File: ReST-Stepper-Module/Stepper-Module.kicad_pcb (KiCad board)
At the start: 2 copper layers, 46 x 32.8 mm, 32 parts

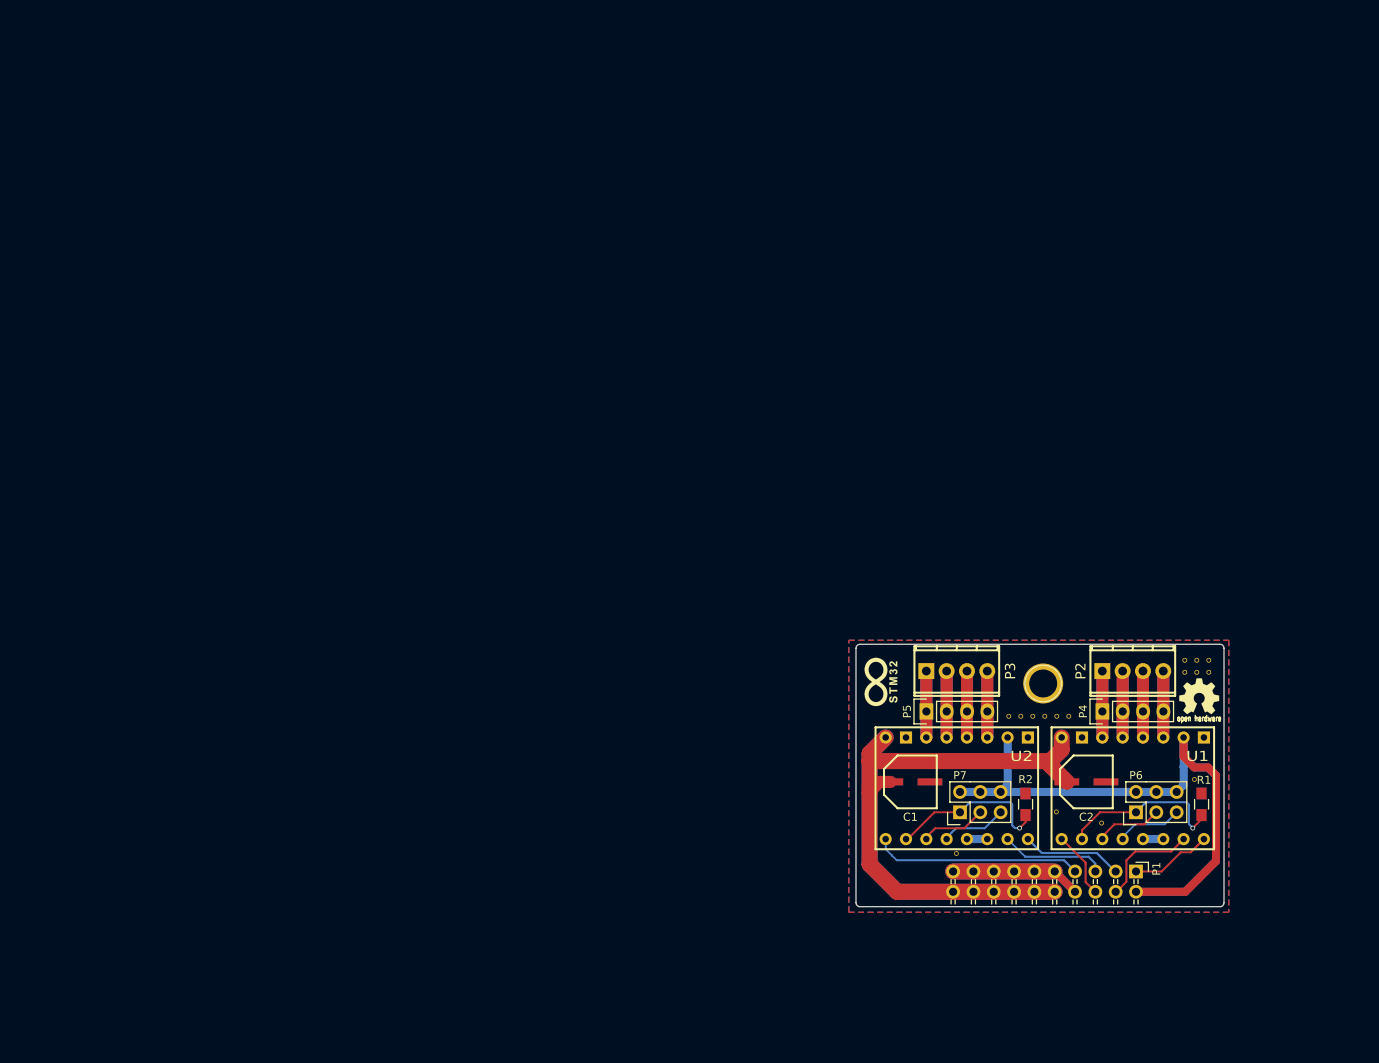
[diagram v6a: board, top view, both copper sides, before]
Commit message: Reworked Modules to sit ontop of the mainboard
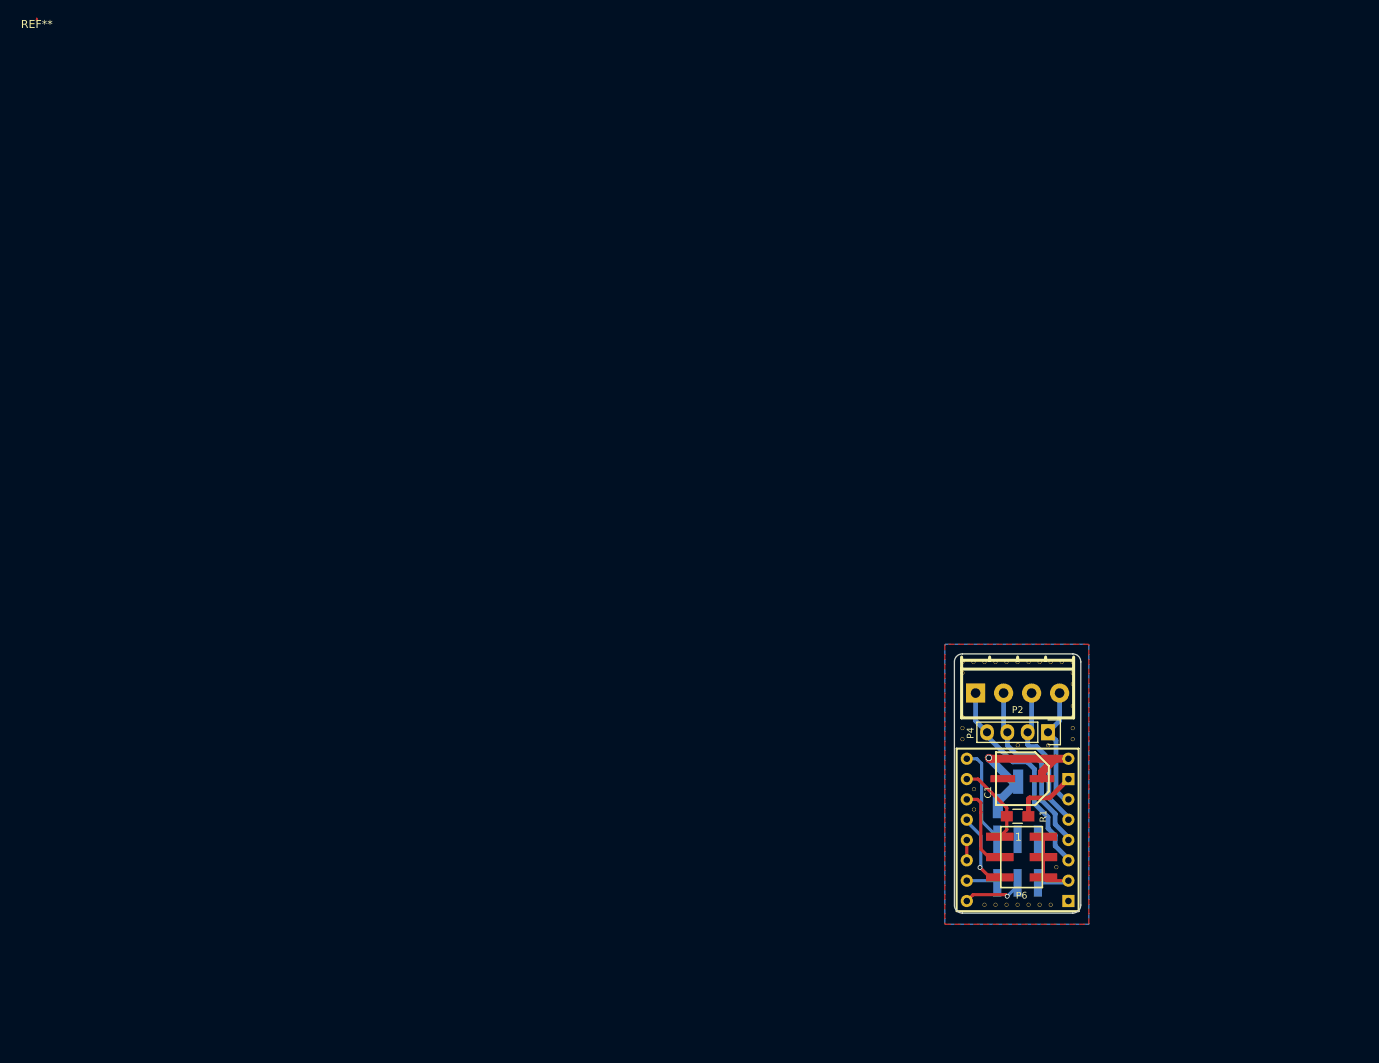
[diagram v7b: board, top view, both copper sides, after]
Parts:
- removed the ? at (144.7, 94.9)
- removed the ? at (143.5, 80.0)
- removed the ? at (129.0, 87.0)
- removed the ? at (127.5, 87.0)
- removed the ? at (126.0, 87.0)
- removed the ? at (124.5, 87.0)
- removed the ? at (123.0, 87.0)
- removed the ? at (105.6, 82.7)
- removed the ? at (145.3, 84.5)
- removed the ? at (125.8, 82.9)
- removed the ? at (121.5, 87.0)
- removed the ? at (133.1, 100.3)
- removed the ? at (115.0, 104.2)
- removed the ? at (127.5, 99.0)
- removed the ? at (146.5, 81.5)
- removed the ? at (145.0, 81.5)
- removed the ? at (143.5, 81.5)
- removed the ? at (146.5, 80.0)
- removed the ? at (145.0, 80.0)
- removed C2: , ReST-Library:CP-PANASONIC-SMT_D8
- removed P5: , Pin_Headers:Pin_Header_Straight_1x04
- removed P7: , Pin_Headers:Pin_Header_Straight_2x03
- removed R2: , Resistors_SMD:R_0805_HandSoldering
- removed U1, U2: , ReST-Library:SWDIP8_.6W
- added ?: , ReST-Library:1pin, F.Cu at (126.4, 90.6)
- added ?: , ReST-Library:1pin, F.Cu at (121.2, 110.6)
- added ?: , ReST-Library:1pin, F.Cu at (119.8, 110.6)
- added ?: , ReST-Library:1pin, F.Cu at (118.5, 110.6)
- added ?: , ReST-Library:1pin, F.Cu at (129.5, 89.9)
- added ?: , ReST-Library:1pin, F.Cu at (129.5, 88.5)
- added ?: , ReST-Library:1pin, F.Cu at (129.5, 87.1)
- added ?: , ReST-Library:1pin, F.Cu at (129.5, 85.7)
- added ?: , ReST-Library:1pin, F.Cu at (129.5, 83.0)
- added ?: , ReST-Library:1pin, F.Cu at (129.5, 81.6)
- added ?: , ReST-Library:1pin, F.Cu at (115.7, 89.9)
- added ?: , ReST-Library:1pin, F.Cu at (122.6, 90.6)
- added ?: , ReST-Library:1pin, F.Cu at (115.7, 88.5)
- added ?: , ReST-Library:1pin, F.Cu at (115.7, 87.1)
- added ?: , ReST-Library:1pin, F.Cu at (115.7, 81.6)
- added ?: , ReST-Library:1pin, F.Cu at (129.5, 80.2)
- added ?: , ReST-Library:1pin, F.Cu at (128.1, 80.2)
- added ?: , ReST-Library:1pin, F.Cu at (126.7, 80.2)
- added ?: , ReST-Library:1pin, F.Cu at (125.4, 80.2)
- added ?: , ReST-Library:1pin, F.Cu at (124.0, 80.2)
- added ?: , ReST-Library:1pin, F.Cu at (122.6, 80.2)
- added ?: , ReST-Library:1pin, F.Cu at (121.2, 80.2)
- added ?: , ReST-Library:1pin, F.Cu at (117.2, 96.1)
- added ?: , ReST-Library:1pin, F.Cu at (119.8, 80.2)
- added ?: , ReST-Library:1pin, F.Cu at (118.5, 80.2)
- added ?: , ReST-Library:1pin, F.Cu at (117.1, 80.2)
- added ?: , ReST-Library:SWDIP8_.6W, F.Cu at (122.6, 101.2)
- added ?: , ReST-Library:1pin, F.Cu at (115.7, 80.2)
- added ?: , ReST-Library:1pin, F.Cu at (117.2, 98.7)
- added ?: , ReST-Library:1pin, F.Cu at (127.4, 105.9)
- added ?: , ReST-Library:1pin, F.Cu at (126.7, 110.6)
- added ?: , ReST-Library:1pin, F.Cu at (125.4, 110.6)
- added ?: , ReST-Library:1pin, F.Cu at (124.0, 110.6)
- added ?: , ReST-Library:1pin, F.Cu at (122.6, 110.6)
- added REF**: muwave_arcstub, muwave_arcstub, F.Cu at (0.00, 0.00)
- P1: footprint ReST-Library:Pin_Header_Angled_2x10 -> ReST-Library:bb02-hy02a; moved to B.Cu
- P2: footprint 2:mpt_0,5%2f4-2,54 -> ReST-Library:pt_1,5-4-3,5-h
- P3: footprint 2:mpt_0,5%2f4-2,54 -> ReST-Library:bb02-hp06; moved to B.Cu
- P6: footprint Pin_Headers:Pin_Header_Straight_2x03 -> ReST-Library:bb02-hp06
- moved P3 24.9 mm to (122.6, 105.1), turned to 0 degrees
- moved R1 23.0 mm to (122.6, 99.5), turned to 0 degrees
- moved P1 18.7 mm to (121.4, 96.7), turned to 180 degrees
- moved P6 15.4 mm to (123.1, 104.6), turned to 270 degrees
- moved P2 14.5 mm to (122.6, 83.4)
- moved C1 14.0 mm to (123.2, 94.8), turned to 180 degrees
- moved P4 7.28 mm to (126.4, 89.0), turned to 270 degrees
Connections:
- P1 pad 1: /E1-DIR -> +12V
- P1 pad 2: +3V3 -> +12V
- P3 pad 1: Net-(P3-Pad1) -> /EN
- P3 pad 2: Net-(P3-Pad2) -> /STEP
- P3 pad 3: Net-(P3-Pad3) -> GND
- P3 pad 4: Net-(P3-Pad4) -> /DIR
- P4 pad 1: Net-(P2-Pad1) -> Net-(P2-Pad4)
- P4 pad 2: Net-(P2-Pad2) -> Net-(P2-Pad3)
- P4 pad 3: Net-(P2-Pad3) -> Net-(P2-Pad2)
- P4 pad 4: Net-(P2-Pad4) -> Net-(P2-Pad1)
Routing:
- net +12V: track 115.4 -> 22.2 mm, vias 0 -> 1
- net +3V3: track 100.8 -> 12.3 mm
- net /E2-EN: track 26.1 -> 0.00 mm
- net GND: track 32.6 -> 8.19 mm
- net Net-(P7-Pad1): track 20.9 -> 0.00 mm, vias 1 -> 0
- net Net-(P3-Pad3): track 16.9 -> 0.00 mm
- net Net-(P3-Pad1): track 16.9 -> 0.00 mm
- net Net-(P3-Pad2): track 16.9 -> 0.00 mm
- net Net-(P3-Pad4): track 16.9 -> 0.00 mm
- net /E2-STEP: track 14.0 -> 0.00 mm
- net /E1-STEP: track 13.3 -> 0.00 mm
- net /E2-DIR: track 12.8 -> 0.00 mm
- net /EN: track 0.00 -> 12.4 mm
- net Net-(P6-Pad1): track 21.3 -> 10.5 mm, vias 1 -> 0
- net /E1-DIR: track 10.2 -> 0.00 mm
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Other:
- board size 46 x 32.8 mm -> 15.8 x 32.4 mm
- board text removed: "ReST32 Stepper Module Rev. A @maker_berry"

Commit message: finishing touches on Heater and Stepper Modules
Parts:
- removed REF**: muwave_arcstub, muwave_arcstub
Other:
- rule pad_to_mask_clearance: 0.2 -> 0
- board text added: "MS1"
